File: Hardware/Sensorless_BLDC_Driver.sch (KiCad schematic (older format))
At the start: 69 parts, among them J1 POWER, J2 MOTOR, Q1 BUK7M15-60EX, Q2 BUK7M15-60EX, Q3 BUK7M15-60EX, Q4 BUK7M15-60EX, Q5 BUK7M15-60EX, Q6 BUK7M15-60EX, U1 PSoC5LP_Prototyping_Kit, U2 FAN7888

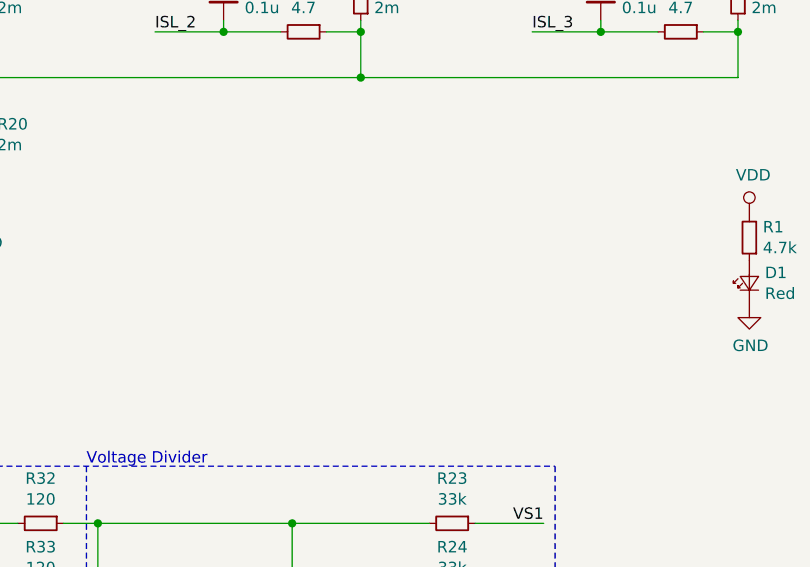
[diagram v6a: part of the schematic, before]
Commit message: [add] add VDD feedback
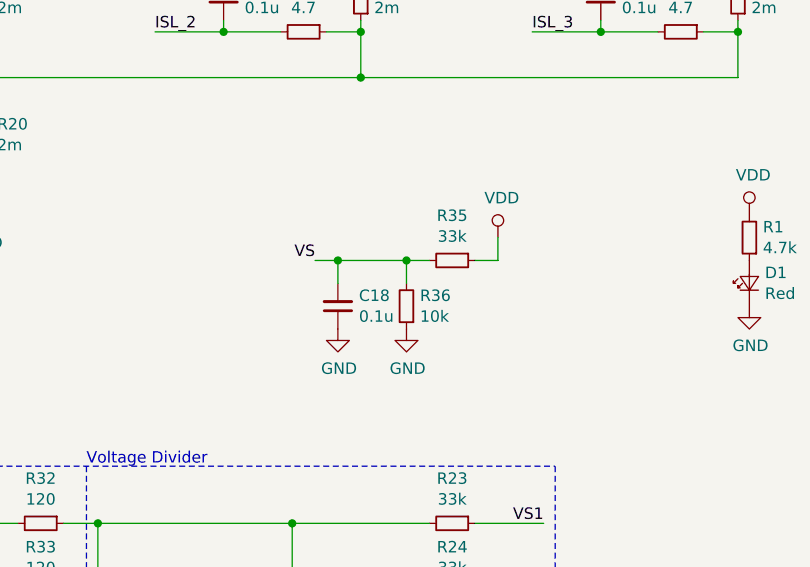
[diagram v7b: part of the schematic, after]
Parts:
- added C18: 0.1u, Capacitor_SMD:C_0402_1005Metric, symbol Device:C_Small
- added R35: 33k, Resistor_SMD:R_0402_1005Metric, symbol Device:R_Small
- added R36: 10k, Resistor_SMD:R_0402_1005Metric, symbol Device:R_Small
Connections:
- net GND: now also C18.1, R36.1
- net VDD: now also R35.1
- new net VS: C18.2, R35.2, R36.2
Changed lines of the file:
@@
 Connection ~ 8650 750
 $Comp
-L power:GND #PWR?
+L power:GND #PWR0102
 U 1 1 5EC07216
 P 8950 950
-F 0 "#PWR?" H 8950 700 50  0001 C CNN
+F 0 "#PWR0102" H 8950 700 50  0001 C CNN
 F 1 "GND" H 8955 777 50  0000 C CNN
 F 2 "" H 8950 950 50  0001 C CNN
@@
 $EndComp
 $Comp
-L power:VDD #PWR?
+L power:VDD #PWR0103
 U 1 1 5EC07660
 P 7000 750
-F 0 "#PWR?" H 7000 600 50  0001 C CNN
+F 0 "#PWR0103" H 7000 600 50  0001 C CNN
 F 1 "VDD" H 7017 923 50  0000 C CNN
 F 2 "" H 7000 750 50  0001 C CNN
@@
 Connection ~ 7000 750
 $Comp
-L power:GND #PWR?
+L power:GND #PWR0121
 U 1 1 5EC07673
 P 7300 950
-F 0 "#PWR?" H 7300 700 50  0001 C CNN
+F 0 "#PWR0121" H 7300 700 50  0001 C CNN
 F 1 "GND" H 7305 777 50  0000 C CNN
 F 2 "" H 7300 950 50  0001 C CNN
@@
 $EndComp
 $Comp
-L power:VDD #PWR?
+L power:VDD #PWR0122
 U 1 1 5EC111A3
 P 5350 750
-F 0 "#PWR?" H 5350 600 50  0001 C CNN
+F 0 "#PWR0122" H 5350 600 50  0001 C CNN
 F 1 "VDD" H 5367 923 50  0000 C CNN
 F 2 "" H 5350 750 50  0001 C CNN
@@
 Connection ~ 5350 750
 $Comp
-L power:GND #PWR?
+L power:GND #PWR0125
 U 1 1 5EC111B6
 P 5650 950
-F 0 "#PWR?" H 5650 700 50  0001 C CNN
+F 0 "#PWR0125" H 5650 700 50  0001 C CNN
 F 1 "GND" H 5655 777 50  0000 C CNN
 F 2 "" H 5650 950 50  0001 C CNN
@@
 	-1   0    0    1
 $EndComp
+$Comp
+L Device:R_Small R35
+U 1 1 5EC26916
+P 7400 3450
+F 0 "R35" V 7204 3450 50  0000 C CNN
+F 1 "33k" V 7295 3450 50  0000 C CNN
+F 2 "Resistor_SMD:R_0402_1005Metric" H 7400 3450 50  0001 C CNN
+F 3 "https://www.mouser.jp/datasheet/2/315/AOA0000C304-1149620.pdf" H 7400 3450 50  0001 C CNN
+F 4 "mouser" H 0   -1150 50  0001 C CNN "Agency"
+F 5 "https://www.mouser.jp/ProductDetail/Panasonic/ERJ-2RKF3302X?qs=sGAEpiMZZMvdGkrng054t8AJgcdMkx7xChk6hee14qQ=" H 0   -1150 50  0001 C CNN "Link"
+F 6 "ERJ-2RKF3302X" H 0   -1150 50  0001 C CNN "MPN"
+	1    7400 3450
+	0    1    1    0
+$EndComp
+$Comp
+L Device:R_Small R36
+U 1 1 5EC26C1E
+P 7200 3650
+F 0 "R36" H 7141 3604 50  0000 R CNN
+F 1 "10k" H 7141 3695 50  0000 R CNN
+F 2 "Resistor_SMD:R_0402_1005Metric" H 7200 3650 50  0001 C CNN
+F 3 "https://b2b-api.panasonic.eu/file_stream/pids/fileversion/1242" H 7200 3650 50  0001 C CNN
+F 4 "Digikey" H 500 -1850 50  0001 C CNN "Agency"
+F 5 "https://www.digikey.jp/product-detail/ja/panasonic-electronic-components/ERJ-2GEJ103X/P10KJCT-ND/146734" H 500 -1850 50  0001 C CNN "Link"
+F 6 "ERJ-2GEJ103X" H 500 -1850 50  0001 C CNN "MPN"
+	1    7200 3650
+	-1   0    0    1
+$EndComp
+$Comp
+L power:GND #PWR?
+U 1 1 5EC3107B
+P 7200 3750
+F 0 "#PWR?" H 7200 3500 50  0001 C CNN
+F 1 "GND" H 7205 3577 50  0000 C CNN
+F 2 "" H 7200 3750 50  0001 C CNN
+F 3 "" H 7200 3750 50  0001 C CNN
+	1    7200 3750
+	1    0    0    -1
+$EndComp
+$Comp
+L power:VDD #PWR?
+U 1 1 5EC31114
+P 7600 3350
+F 0 "#PWR?" H 7600 3200 50  0001 C CNN
+F 1 "VDD" H 7617 3523 50  0000 C CNN
+F 2 "" H 7600 3350 50  0001 C CNN
+F 3 "" H 7600 3350 50  0001 C CNN
+	1    7600 3350
+	1    0    0    -1
+$EndComp
+Wire Wire Line
+	7600 3350 7600 3450
+Wire Wire Line
+	7600 3450 7500 3450
+Wire Wire Line
+	7200 3550 7200 3450
+Wire Wire Line
+	7200 3450 7300 3450
+Connection ~ 7200 3450
+Text Label 6800 3450 2    50   ~ 0
+VS
+$Comp
+L Device:C_Small C18
+U 1 1 5EC64C4E
+P 6900 3650
+F 0 "C18" H 6808 3604 50  0000 R CNN
+F 1 "0.1u" H 6808 3695 50  0000 R CNN
+F 2 "Capacitor_SMD:C_0402_1005Metric" H 6900 3650 50  0001 C CNN
+F 3 "https://search.murata.co.jp/Ceramy/image/img/A01X/G101/ENG/GRM155R62A104KE14-01.pdf" H 6900 3650 50  0001 C CNN
+F 4 "Digikey" H 500 1350 50  0001 C CNN "Agency"
+F 5 "https://www.digikey.jp/product-detail/ja/murata-electronics/GRM155R62A104KE14D/490-10458-1-ND/5026370" H 500 1350 50  0001 C CNN "Link"
+F 6 "GRM155R62A104KE14D" H 500 1350 50  0001 C CNN "MPN"
+	1    6900 3650
+	-1   0    0    1
+$EndComp
+Wire Wire Line
+	6800 3450 6900 3450
+Wire Wire Line
+	6900 3450 6900 3550
+Connection ~ 6900 3450
+Wire Wire Line
+	6900 3450 7200 3450
+$Comp
+L power:GND #PWR?
+U 1 1 5EC84488
+P 6900 3750
+F 0 "#PWR?" H 6900 3500 50  0001 C CNN
+F 1 "GND" H 6905 3577 50  0000 C CNN
+F 2 "" H 6900 3750 50  0001 C CNN
+F 3 "" H 6900 3750 50  0001 C CNN
+	1    6900 3750
+	1    0    0    -1
+$EndComp
 $EndSCHEMATC

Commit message: [update] change power connector from DF63 to DF22
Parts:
- J1: footprint Connector_Hirose:Hirose_DF63M-2P-3.96DSA_1x02_P3.96mm_Vertical -> KUTKiCad_footprint:Hirose_DF22_DF22x-2P-7.92DSA_1x02_P7.92mm_Vertical; Agency mouser -> (none); Link https://www.mouser.jp/ProductDetail/Hirose-Connector/DF63M-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 -> (none); MPN DF63M-2P-3.96DSA -> DF22-3P-7.92DSA
- J2: footprint Connector_Hirose:Hirose_DF63M-3P-3.96DSA_1x03_P3.96mm_Vertical -> KUTKiCad_footprint:Hirose_DF22_DF22x-3P-7.92DSA_1x03_P7.92mm_Vertical; Agency mouser -> (none); Link https://www.mouser.jp/ProductDetail/Hirose-Connector/DF63M-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 -> (none); MPN DF63M-3P-3.96DSA -> DF22-3P-7.92DSA
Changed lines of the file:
@@
 F 0 "J2" H 10023 3730 50  0000 R CNN
 F 1 "MOTOR" H 10023 3821 50  0000 R CNN
-F 2 "Connector_Hirose:Hirose_DF63M-3P-3.96DSA_1x03_P3.96mm_Vertical" H 10050 3800 50  0001 C CNN
-F 3 "https://www.hirose.com/product/document?clcode=&productname=&series=DF63&documenttype=Catalog&lang=en&documentid=D31622_ja" H 10050 3800 50  0001 C CNN
-F 4 "mouser" H 0   0   50  0001 C CNN "Agency"
-F 5 "https://www.mouser.jp/ProductDetail/Hirose-Connector/DF63M-3P-396DSA?qs=sGAEpiMZZMvlX3nhDDO4ADf%252Bp9sbtHSJ34uorugIvF4%3D" H 0   0   50  0001 C CNN "Link"
-F 6 "DF63M-3P-3.96DSA" H 0   0   50  0001 C CNN "MPN"
+F 2 "KUTKiCad_footprint:Hirose_DF22_DF22x-3P-7.92DSA_1x03_P7.92mm_Vertical" H 10050 3800 50  0001 C CNN
+F 3 "" H 10050 3800 50  0001 C CNN
+F 4 "DF22-3P-7.92DSA" H 0   0   50  0001 C CNN "MPN"
 	1    10050 3800
 	-1   0    0    1
@@
 F 0 "J1" H 10022 3073 50  0000 R CNN
 F 1 "POWER" H 10022 2982 50  0000 R CNN
-F 2 "Connector_Hirose:Hirose_DF63M-2P-3.96DSA_1x02_P3.96mm_Vertical" H 10050 3100 50  0001 C CNN
-F 3 "https://www.hirose.com/product/document?clcode=&productname=&series=DF63&documenttype=Catalog&lang=en&documentid=D31622_ja" H 10050 3100 50  0001 C CNN
-F 4 "mouser" H 0   0   50  0001 C CNN "Agency"
-F 5 "https://www.mouser.jp/ProductDetail/Hirose-Connector/DF63M-2P-396DSA?qs=sGAEpiMZZMuyN6ZGvFhteTZk7n8ferJ4dPrvZ0xUyi6TkXnGsFceHw%3D%3D" H 0   0   50  0001 C CNN "Link"
-F 6 "DF63M-2P-3.96DSA" H 0   0   50  0001 C CNN "MPN"
+F 2 "KUTKiCad_footprint:Hirose_DF22_DF22x-2P-7.92DSA_1x02_P7.92mm_Vertical" H 10050 3100 50  0001 C CNN
+F 3 "" H 10050 3100 50  0001 C CNN
+F 4 "DF22-3P-7.92DSA" H 0   0   50  0001 C CNN "MPN"
 	1    10050 3100
 	-1   0    0    -1
